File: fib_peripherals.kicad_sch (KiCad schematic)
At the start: 0 parts

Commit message: added several ICs, implementted schematics for charger, boost converter and LDOs
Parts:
- added J1, J4: Conn_02x20_Odd_Even, symbol Connector_Generic:Conn_02x20_Odd_Even
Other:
- note added: "GROVE"
- note added: "I2C"
- note added: "IT8951"
- note added: "SPI"
- note added: "UART"
- note added: "UART2"

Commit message: added symbol&footprint for orin/sodimm, added a bunch of specs and docs, partially implemented audio, full steam ahead
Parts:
- J1, J4: footprint (none) -> Connector_PinHeader_2.54mm:PinHeader_2x20_P2.54mm_Vertical
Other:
- moved on the sheet: J4
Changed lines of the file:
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@@
 	(text "IT8951"
 		(exclude_from_sim no)
-		(at 77.724 88.646 0)
+		(at 43.434 172.466 0)
 		(effects
 			(font
@@
 	(text "I2C"
 		(exclude_from_sim no)
-		(at 139.446 48.768 0)
+		(at 128.778 39.116 0)
 		(effects
 			(font
@@
 	(text "UART"
 		(exclude_from_sim no)
-		(at 139.954 56.896 0)
+		(at 129.794 44.196 0)
 		(effects
 			(font
@@
 	(text "GROVE"
 		(exclude_from_sim no)
-		(at 140.97 76.708 0)
+		(at 130.81 64.008 0)
 		(effects
 			(font
@@
 	(text "UART2"
 		(exclude_from_sim no)
-		(at 140.462 66.04 0)
+		(at 130.302 53.34 0)
 		(effects
 			(font
@@
 	(text "SPI"
 		(exclude_from_sim no)
-		(at 139.7 41.656 0)
+		(at 128.778 32.766 0)
 		(effects
 			(font
@@
 			)
 		)
-		(property "Footprint" ""
+		(property "Footprint" "Connector_PinHeader_2.54mm:PinHeader_2x20_P2.54mm_Vertical"
 			(at 41.91 57.15 0)
 			(effects
@@
 	(symbol
 		(lib_id "Connector_Generic:Conn_02x20_Odd_Even")
-		(at 76.2 57.15 0)
+		(at 41.91 140.97 0)
 		(unit 1)
 		(exclude_from_sim no)
@@
 		(fields_autoplaced yes)
 		(property "Reference" "J4"
-			(at 77.47 27.94 0)
+			(at 43.18 111.76 0)
 			(effects
 				(font
@@
 		)
 		(property "Value" "Conn_02x20_Odd_Even"
-			(at 77.47 30.48 0)
-			(effects
-				(font
-					(size 1.27 1.27)
-				)
-			)
-		)
-		(property "Footprint" ""
-			(at 76.2 57.15 0)
+			(at 43.18 114.3 0)
+			(effects
+				(font
+					(size 1.27 1.27)
+				)
+			)
+		)
+		(property "Footprint" "Connector_PinHeader_2.54mm:PinHeader_2x20_P2.54mm_Vertical"
+			(at 41.91 140.97 0)
 			(effects
 				(font
@@
 		)
 		(property "Datasheet" "~"
-			(at 76.2 57.15 0)
+			(at 41.91 140.97 0)
 			(effects
 				(font
@@
 		)
 		(property "Description" "Generic connector, double row, 02x20, odd/even pin numbering scheme (row 1 odd numbers, row 2 even numbers), script generated (kicad-library-utils/schlib/autogen/connector/)"
-			(at 76.2 57.15 0)
-			(effects
-				(font
+			(at 41.91 140.97 0)
+			(effects
+				(font

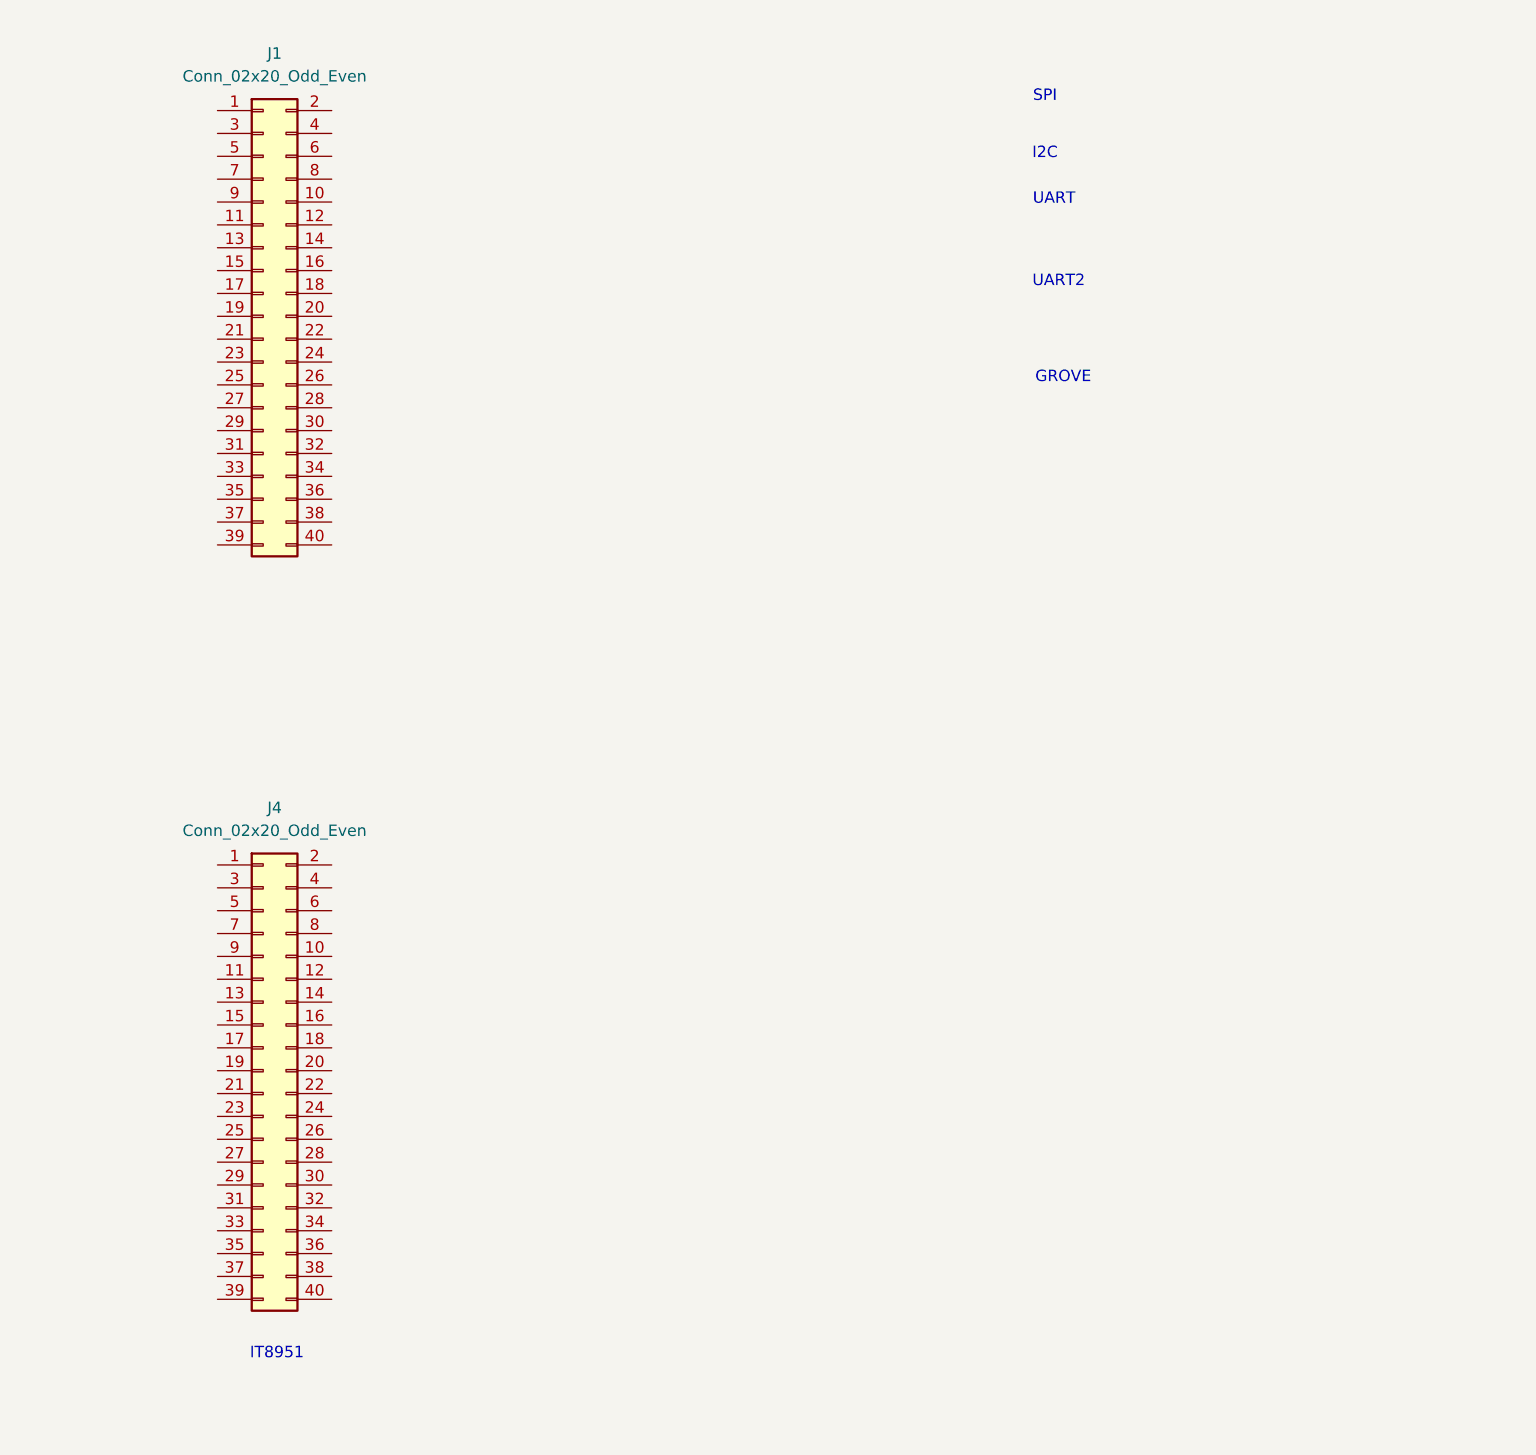
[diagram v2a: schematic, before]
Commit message: added nets for 40 pin headers (epd & rpi header) connected some of the nets i'm reeusing
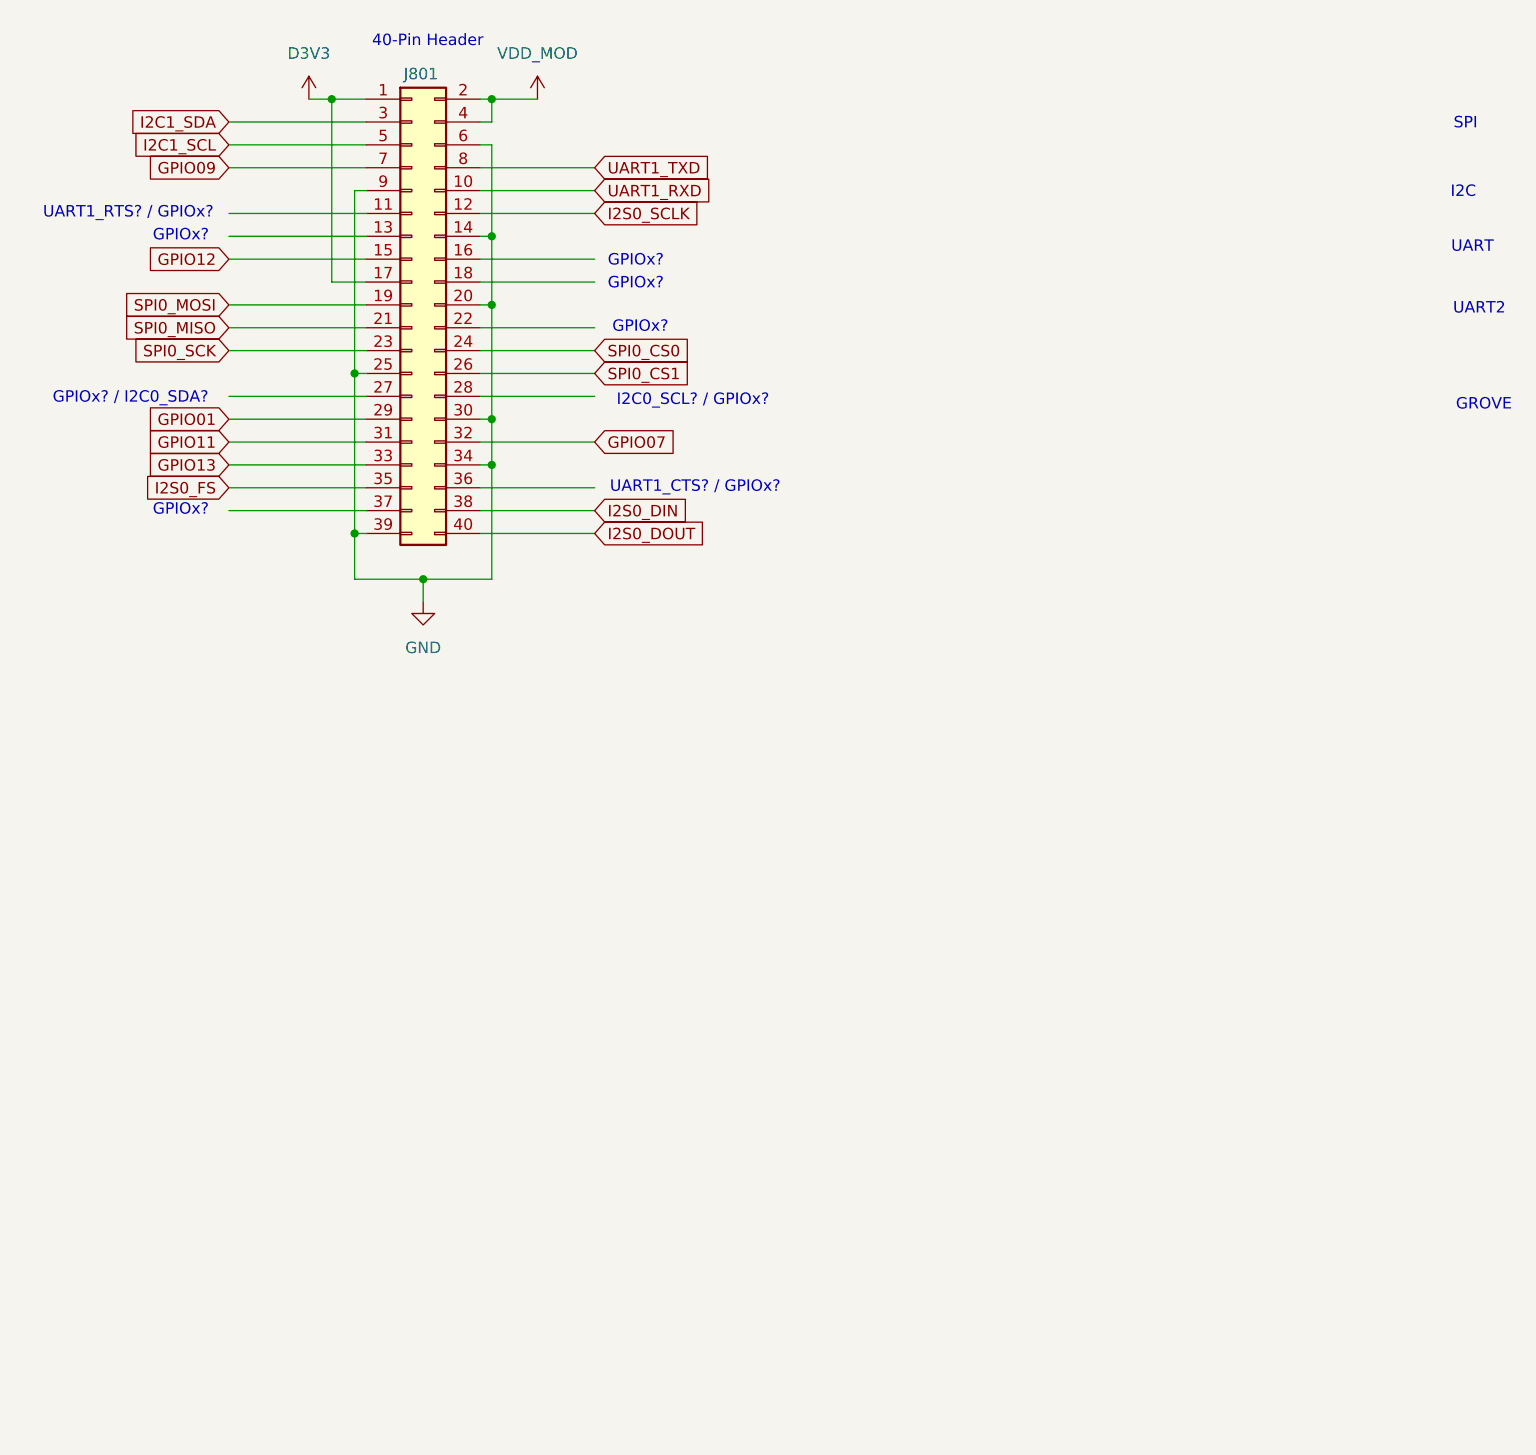
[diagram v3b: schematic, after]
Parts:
- removed J1: Conn_02x20_Odd_Even, Connector_PinHeader_2.54mm:PinHeader_2x20_P2.54mm_Vertical, symbol Connector_Generic:Conn_02x20_Odd_Even
- renumbered J4 to J801
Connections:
- net D3V3: now reaches J801.1 (Pin_1)
- net D3V3: now also J801.17 (Pin_17)
- net UART1_RXD: now reaches J801.10 (Pin_10)
- net I2S0_SCLK: now reaches J801.12 (Pin_12)
- net GND: now reaches J801.14 (Pin_14)
- net GND: now also J801.20 (Pin_20), J801.25 (Pin_25), J801.30 (Pin_30), J801.34 (Pin_34), J801.39 (Pin_39), J801.6 (Pin_6), J801.9 (Pin_9)
- net GPIO12: now reaches J801.15 (Pin_15)
- net SPI0_MOSI: now reaches J801.19 (Pin_19)
- net VDD_MOD: now reaches J801.2 (Pin_2)
- net VDD_MOD: now also J801.4 (Pin_4)
- net SPI0_MISO: now reaches J801.21 (Pin_21)
- net SPI0_SCK: now reaches J801.23 (Pin_23)
- net SPI0_CS0: now reaches J801.24 (Pin_24)
- net SPI0_CS1: now reaches J801.26 (Pin_26)
- net GPIO01: now reaches J801.29 (Pin_29)
- net I2C1_SDA: now reaches J801.3 (Pin_3)
- net GPIO11: now reaches J801.31 (Pin_31)
- net GPIO07: now reaches J801.32 (Pin_32)
- net GPIO13: now reaches J801.33 (Pin_33)
- net I2S0_FS: now reaches J801.35 (Pin_35)
- net I2S0_DIN: now reaches J801.38 (Pin_38)
- net I2S0_DOUT: now reaches J801.40 (Pin_40)
- net I2C1_SCL: now reaches J801.5 (Pin_5)
- net GPIO09: now reaches J801.7 (Pin_7)
- net UART1_TXD: now reaches J801.8 (Pin_8)
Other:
- note added: "40-Pin Header"
- note added: "GPIOx?"
- note added: "GPIOx? / I2C0_SDA?"
- note added: "I2C0_SCL? / GPIOx?"
- note added: "UART1_CTS? / GPIOx?"
- note added: "UART1_RTS? / GPIOx?"
- note removed: "IT8951"
- moved on the sheet: J801

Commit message: restructured EPD side of things, replaced rp2040 with esp32 s3 because of it's LCD controller, USB, LP WIFI_BT & EPDiy compat, repurposed USB0 for ESP interfacing, added e-ink pmic
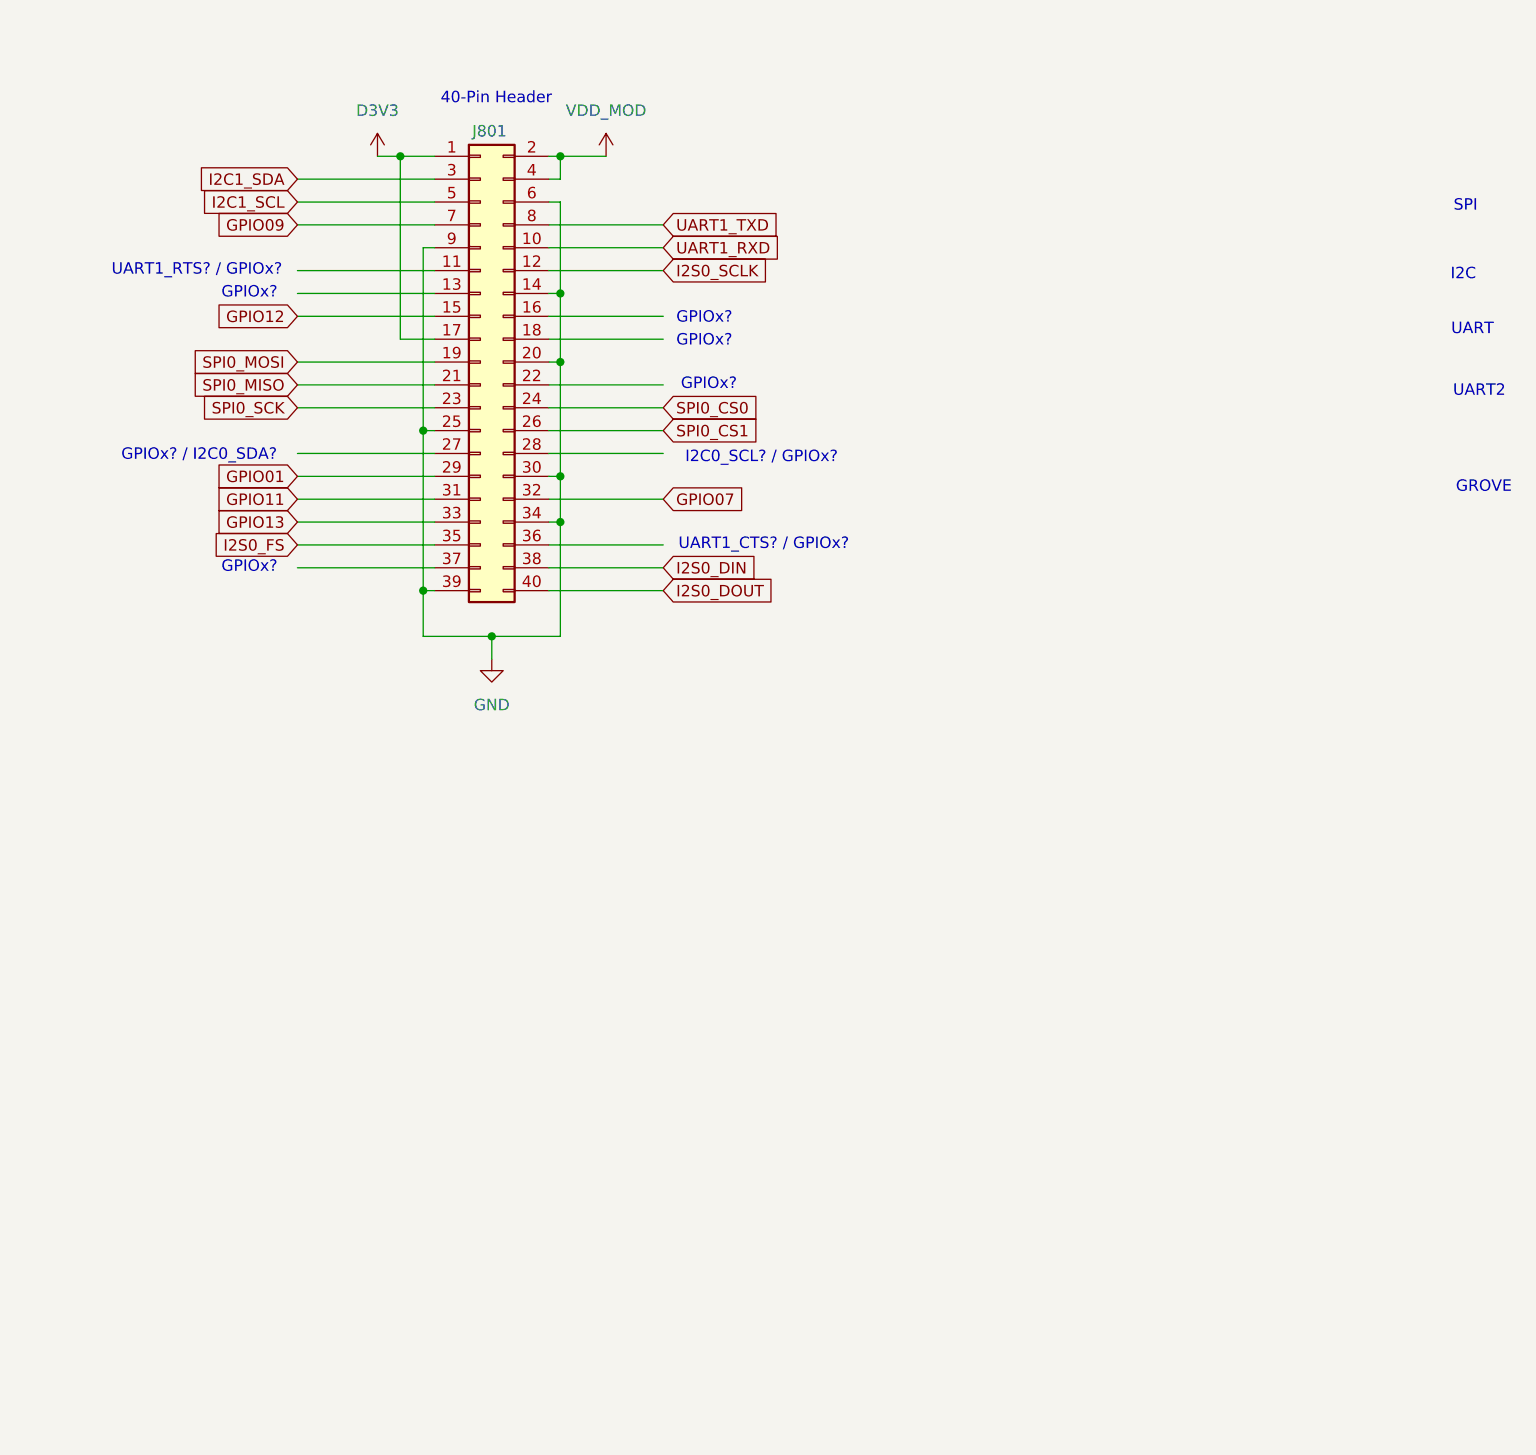
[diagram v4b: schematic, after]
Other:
- moved on the sheet: J801
